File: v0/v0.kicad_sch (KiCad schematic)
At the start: 2 parts, among them CON1 SNES-CONN

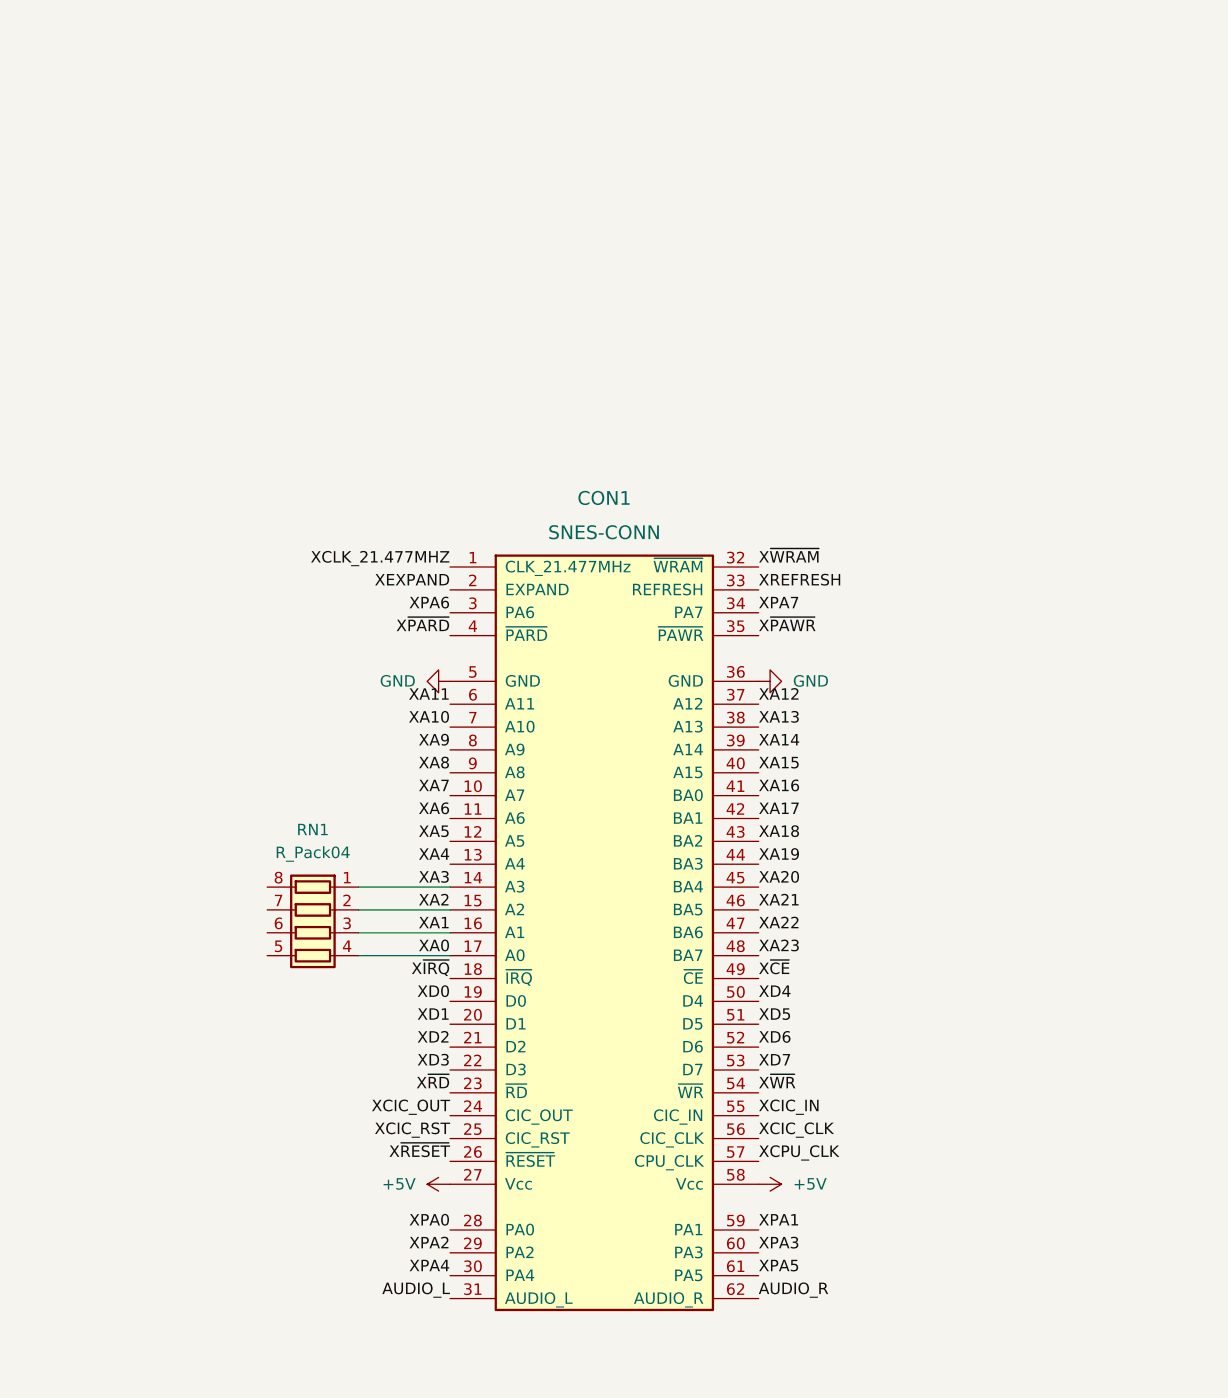
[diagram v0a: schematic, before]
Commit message: Routed shift registers
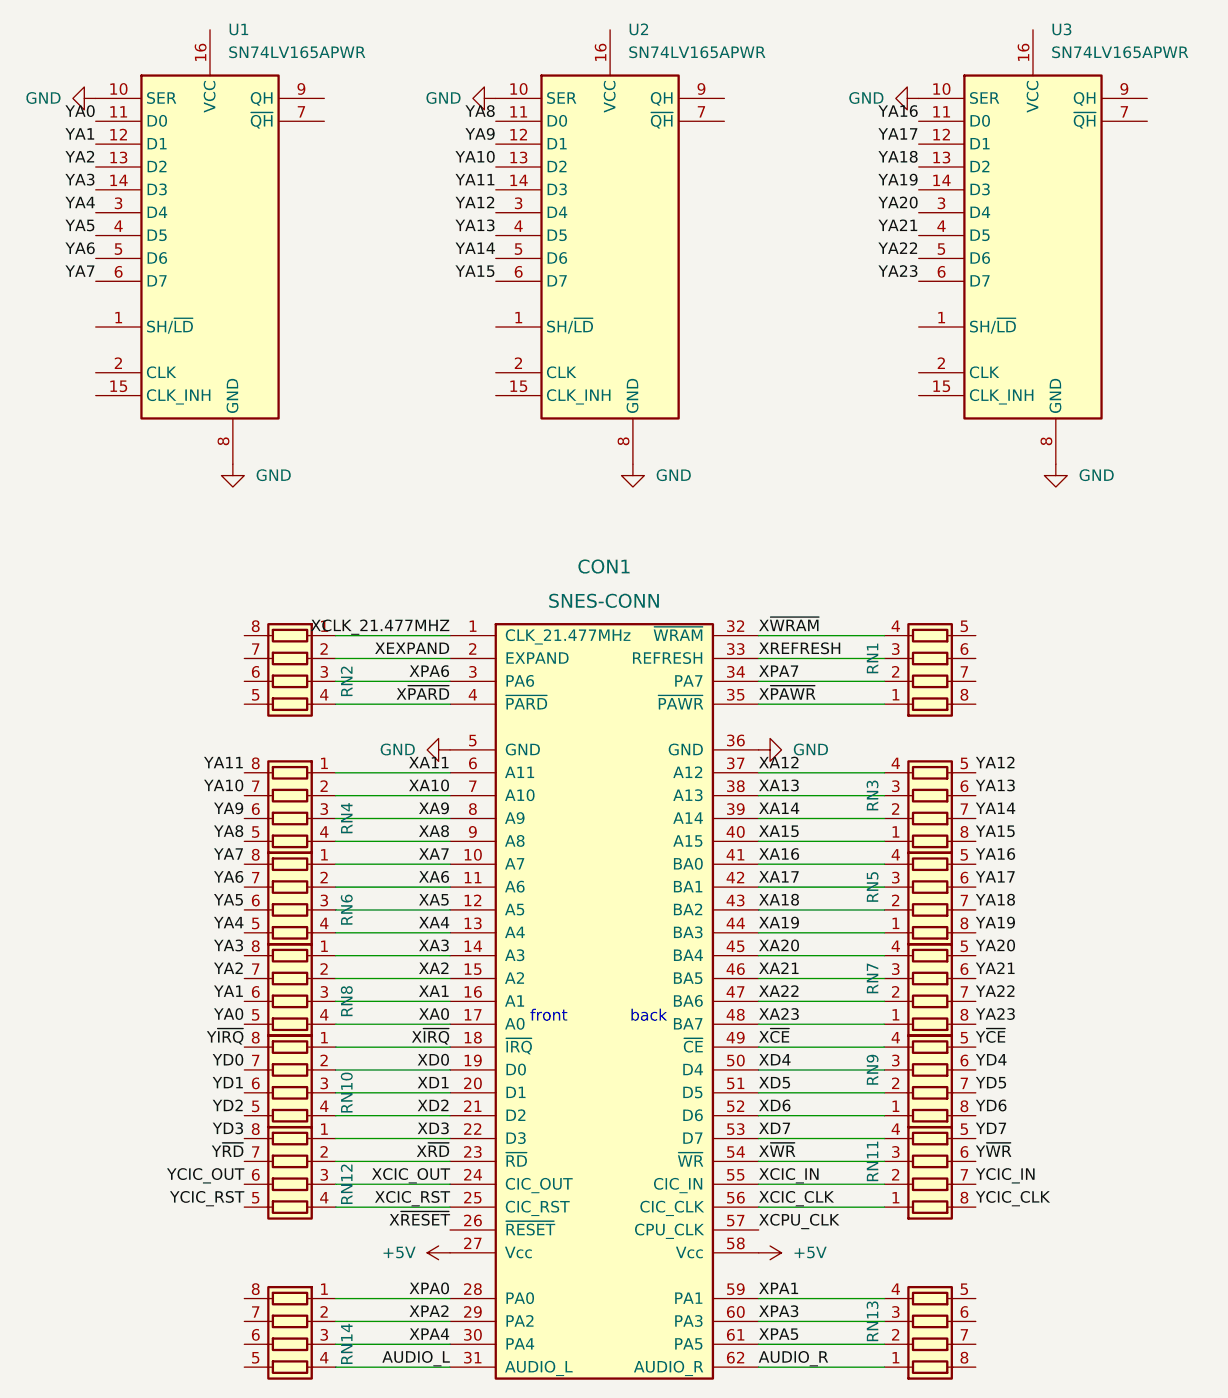
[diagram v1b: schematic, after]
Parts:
- added RN1, RN10, RN11, RN12, RN13, RN14, RN2, RN3, RN4, RN5, RN6, RN7, RN9: R_Pack04, Resistor_SMD:R_Array_Convex_4x1206, symbol Device:R_Pack04
- added U1, U2, U3: SN74LV165APWR, Package_SO:TSSOP-16_4.4x5mm_P0.65mm, symbol 74xx:74HC165
- renumbered RN1 to RN8
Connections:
- net AUDIO_L: now also RN14.4 (R4.1)
- net AUDIO_R: now also RN13.1 (R1.1)
- net GND: now also U1.10 (SER), U1.8 (GND), U2.10 (SER), U2.8 (GND), U3.10 (SER), U3.8 (GND)
- net XA10: now also RN4.2 (R2.1)
- net XA11: now also RN4.1 (R1.1)
- net XA12: now also RN3.4 (R4.1)
- net XA13: now also RN3.3 (R3.1)
- net XA14: now also RN3.2 (R2.1)
- net XA15: now also RN3.1 (R1.1)
- net XA16: now also RN5.4 (R4.1)
- net XA17: now also RN5.3 (R3.1)
- net XA18: now also RN5.2 (R2.1)
- net XA19: now also RN5.1 (R1.1)
- net XA20: now also RN7.4 (R4.1)
- net XA21: now also RN7.3 (R3.1)
- net XA22: now also RN7.2 (R2.1)
- net XA23: now also RN7.1 (R1.1)
- net XA4: now also RN6.4 (R4.1)
- net XA5: now also RN6.3 (R3.1)
- net XA6: now also RN6.2 (R2.1)
- net XA7: now also RN6.1 (R1.1)
- net XA8: now also RN4.4 (R4.1)
- net XA9: now also RN4.3 (R3.1)
- net XCIC_CLK: now also RN11.1 (R1.1)
- net XCIC_IN: now also RN11.2 (R2.1)
- net XCIC_OUT: now also RN12.3 (R3.1)
- net XCIC_RST: now also RN12.4 (R4.1)
- net XCLK_21.477MHZ: now also RN2.1 (R1.1)
- net XD0: now also RN10.2 (R2.1)
- net XD1: now also RN10.3 (R3.1)
- net XD2: now also RN10.4 (R4.1)
- net XD3: now also RN12.1 (R1.1)
- net XD4: now also RN9.3 (R3.1)
- net XD5: now also RN9.2 (R2.1)
- net XD6: now also RN9.1 (R1.1)
- net XD7: now also RN11.4 (R4.1)
- net XEXPAND: now also RN2.2 (R2.1)
- net XPA0: now also RN14.1 (R1.1)
- net XPA1: now also RN13.4 (R4.1)
- net XPA2: now also RN14.2 (R2.1)
- net XPA3: now also RN13.3 (R3.1)
- net XPA4: now also RN14.3 (R3.1)
- net XPA5: now also RN13.2 (R2.1)
- net XPA6: now also RN2.3 (R3.1)
- net XPA7: now also RN1.2 (R2.1)
- net XREFRESH: now also RN1.3 (R3.1)
- net X~{CE}: now also RN9.4 (R4.1)
- net X~{IRQ}: now also RN10.1 (R1.1)
- net X~{PARD}: now also RN2.4 (R4.1)
- net X~{PAWR}: now also RN1.1 (R1.1)
- net X~{RD}: now also RN12.2 (R2.1)
- net X~{WRAM}: now also RN1.4 (R4.1)
- net X~{WR}: now also RN11.3 (R3.1)
- net YA0: now reaches RN8.5 (R4.2)
- net YA0: now also U1.11 (D0)
- net YA1: now reaches RN8.6 (R3.2)
- net YA1: now also U1.12 (D1)
- net YA2: now reaches RN8.7 (R2.2)
- net YA2: now also U1.13 (D2)
- net YA3: now reaches RN8.8 (R1.2)
- net YA3: now also U1.14 (D3)
- new net YA10: RN4.7 (R2.2), U2.13 (D2)
- new net YA11: RN4.8 (R1.2), U2.14 (D3)
- new net YA12: RN3.5 (R4.2), U2.3 (D4)
- new net YA13: RN3.6 (R3.2), U2.4 (D5)
- new net YA14: RN3.7 (R2.2), U2.5 (D6)
- new net YA15: RN3.8 (R1.2), U2.6 (D7)
- new net YA16: RN5.5 (R4.2), U3.11 (D0)
- new net YA17: RN5.6 (R3.2), U3.12 (D1)
- new net YA18: RN5.7 (R2.2), U3.13 (D2)
- new net YA19: RN5.8 (R1.2), U3.14 (D3)
- new net YA20: RN7.5 (R4.2), U3.3 (D4)
- new net YA21: RN7.6 (R3.2), U3.4 (D5)
- new net YA22: RN7.7 (R2.2), U3.5 (D6)
- new net YA23: RN7.8 (R1.2), U3.6 (D7)
- new net YA4: RN6.5 (R4.2), U1.3 (D4)
- new net YA5: RN6.6 (R3.2), U1.4 (D5)
- new net YA6: RN6.7 (R2.2), U1.5 (D6)
- new net YA7: RN6.8 (R1.2), U1.6 (D7)
- new net YA8: RN4.5 (R4.2), U2.11 (D0)
- new net YA9: RN4.6 (R3.2), U2.12 (D1)
- new net YCIC_CLK: RN11.8 (R1.2)
- new net YCIC_IN: RN11.7 (R2.2)
- new net YCIC_OUT: RN12.6 (R3.2)
- new net YCIC_RST: RN12.5 (R4.2)
- new net YD0: RN10.7 (R2.2)
- new net YD1: RN10.6 (R3.2)
- new net YD2: RN10.5 (R4.2)
- new net YD3: RN12.8 (R1.2)
- new net YD4: RN9.6 (R3.2)
- new net YD5: RN9.7 (R2.2)
- new net YD6: RN9.8 (R1.2)
- new net YD7: RN11.5 (R4.2)
- new net Y~{CE}: RN9.5 (R4.2)
- new net Y~{IRQ}: RN10.8 (R1.2)
- new net Y~{RD}: RN12.7 (R2.2)
- new net Y~{WR}: RN11.6 (R3.2)
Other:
- note added: "back"
- note added: "front"
- moved on the sheet: CON1, RN8

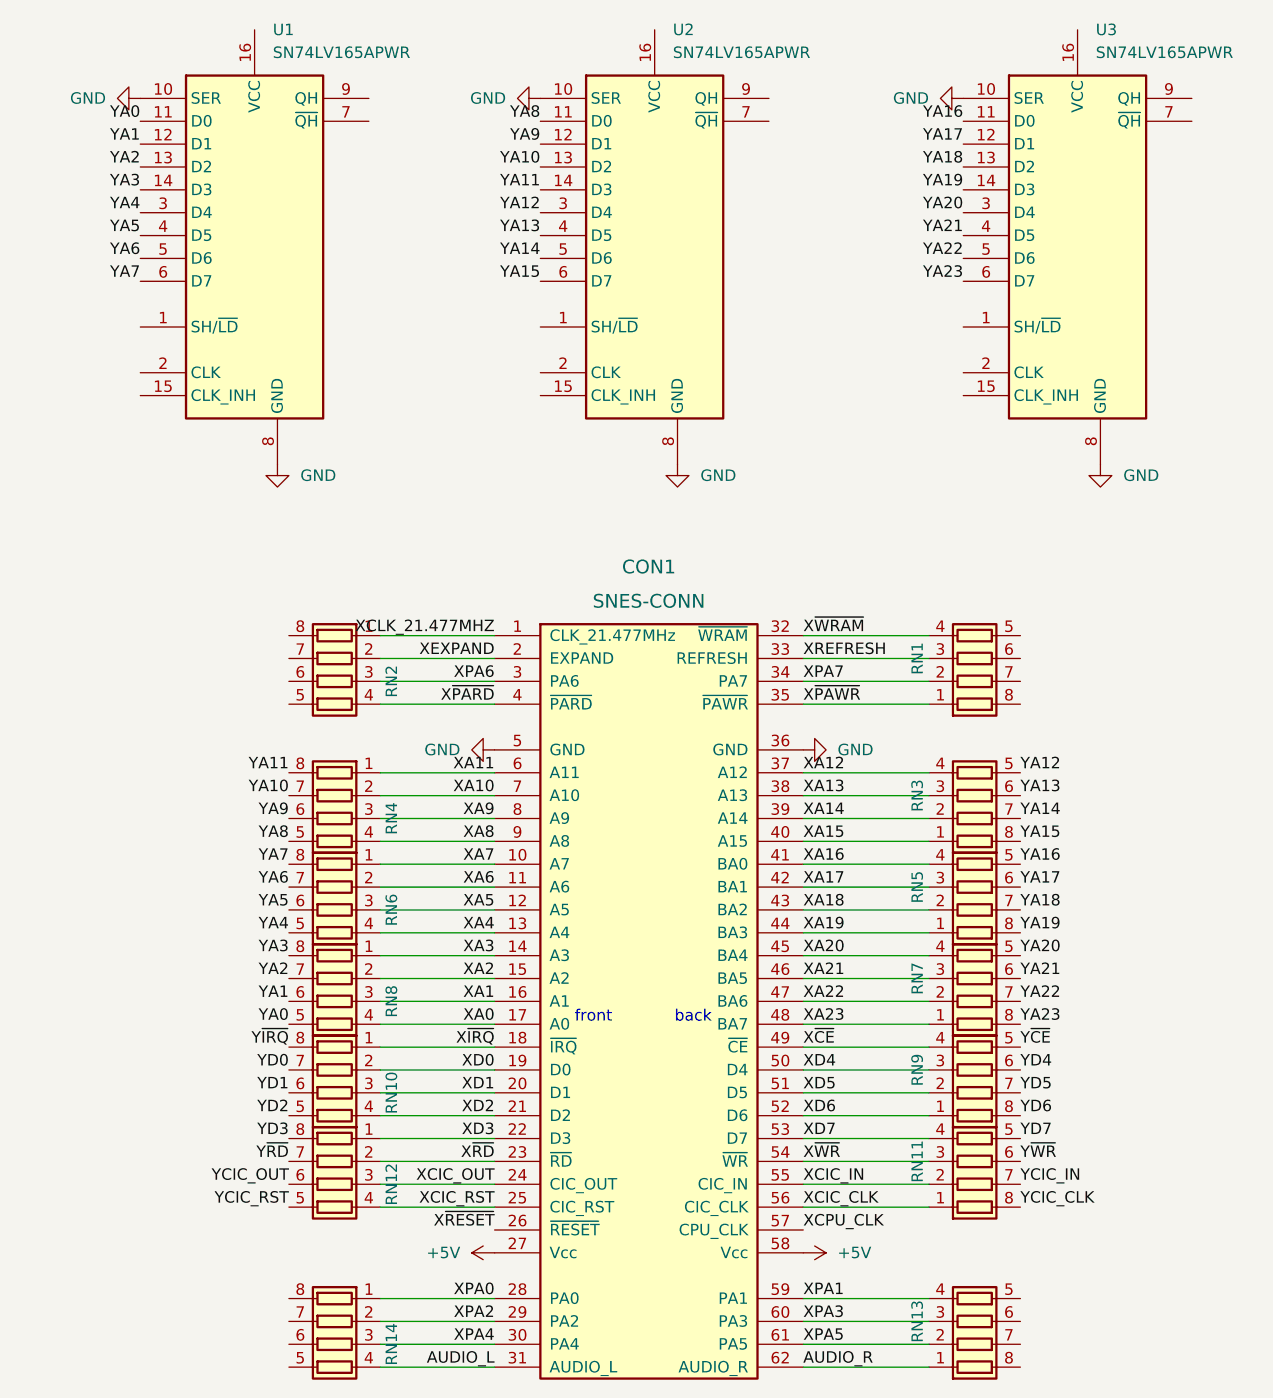
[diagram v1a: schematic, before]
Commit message: Route through 100R networks and into shift registers for address lines
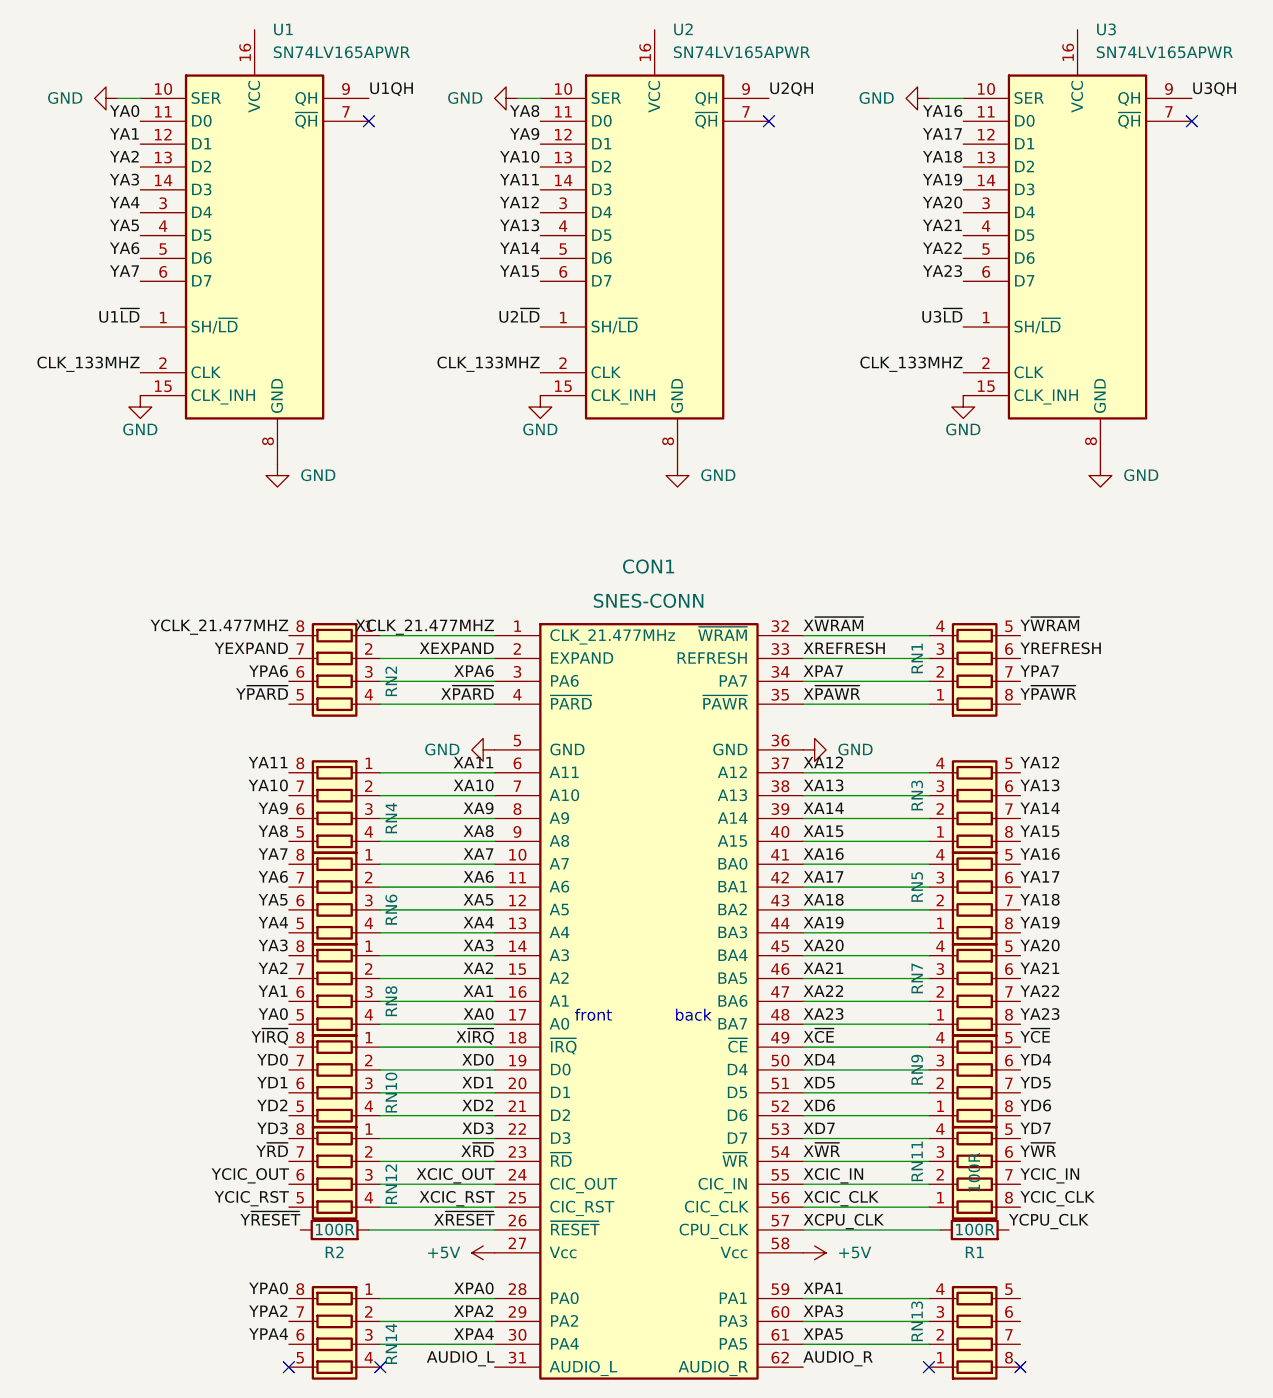
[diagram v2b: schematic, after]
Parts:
- added R1, R2: 100R, Resistor_SMD:R_1206_3216Metric_Pad1.30x1.75mm_HandSolder, symbol Device:R
- RN11, RN9: value R_Pack04 -> 100R
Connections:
- net AUDIO_L: no longer RN14.4 (R4.1)
- net AUDIO_R: no longer RN13.1 (R1.1)
- net GND: now also U1.15 (CLK_INH), U2.15 (CLK_INH), U3.15 (CLK_INH)
- net XCPU_CLK: now also R1.1
- net X~{RESET}: now also R2.2
- net U3~{LD}: now reaches U3.1 (SH/~{LD})
- net CLK_133MHZ: now reaches U3.2 (CLK)
- net CLK_133MHZ: now also U1.2 (CLK), U2.2 (CLK)
- net U3QH: now reaches U3.9 (QH)
- net U2~{LD}: now reaches U2.1 (SH/~{LD})
- net U2QH: now reaches U2.9 (QH)
- net Y~{PARD}: now reaches RN2.5 (R4.2)
- net YPA6: now reaches RN2.6 (R3.2)
- net YEXPAND: now reaches RN2.7 (R2.2)
- net YCLK_21.477MHZ: now reaches RN2.8 (R1.2)
- net U1~{LD}: now reaches U1.1 (SH/~{LD})
- net U1QH: now reaches U1.9 (QH)
- net YPA4: now reaches RN14.6 (R3.2)
- net YPA2: now reaches RN14.7 (R2.2)
- net YPA0: now reaches RN14.8 (R1.2)
- net Y~{WRAM}: now reaches RN1.5 (R4.2)
- net YREFRESH: now reaches RN1.6 (R3.2)
- net YPA7: now reaches RN1.7 (R2.2)
- net Y~{PAWR}: now reaches RN1.8 (R1.2)
- new net YCPU_CLK: R1.2
- new net Y~{RESET}: R2.1
- no-connect marks 0 -> 7
